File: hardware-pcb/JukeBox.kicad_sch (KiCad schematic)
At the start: 80 parts, among them J1 USB_C_Receptacle_USB2.0_16P, J2 Conn_01x04_Pin, Q1 Q_NPN_BEC, SW1 SW_SPST, SW10 SW_SPST, SW11 SW_SPST, SW12 SW_SPST, SW2 SW_SPST, SW3 SW_SPST, SW4 SW_SPST, SW5 SW_SPST, SW6 SW_SPST, SW7 SW_SPST, SW8 SW_SPST, SW9 SW_SPST, U1 NCP1117-3.3_SOT223, U2 W25Q64JVSSIQ-TR, U3 RP2040, U4 st7789v, U5 CAT24C512, Y2 ABM8-272-T3

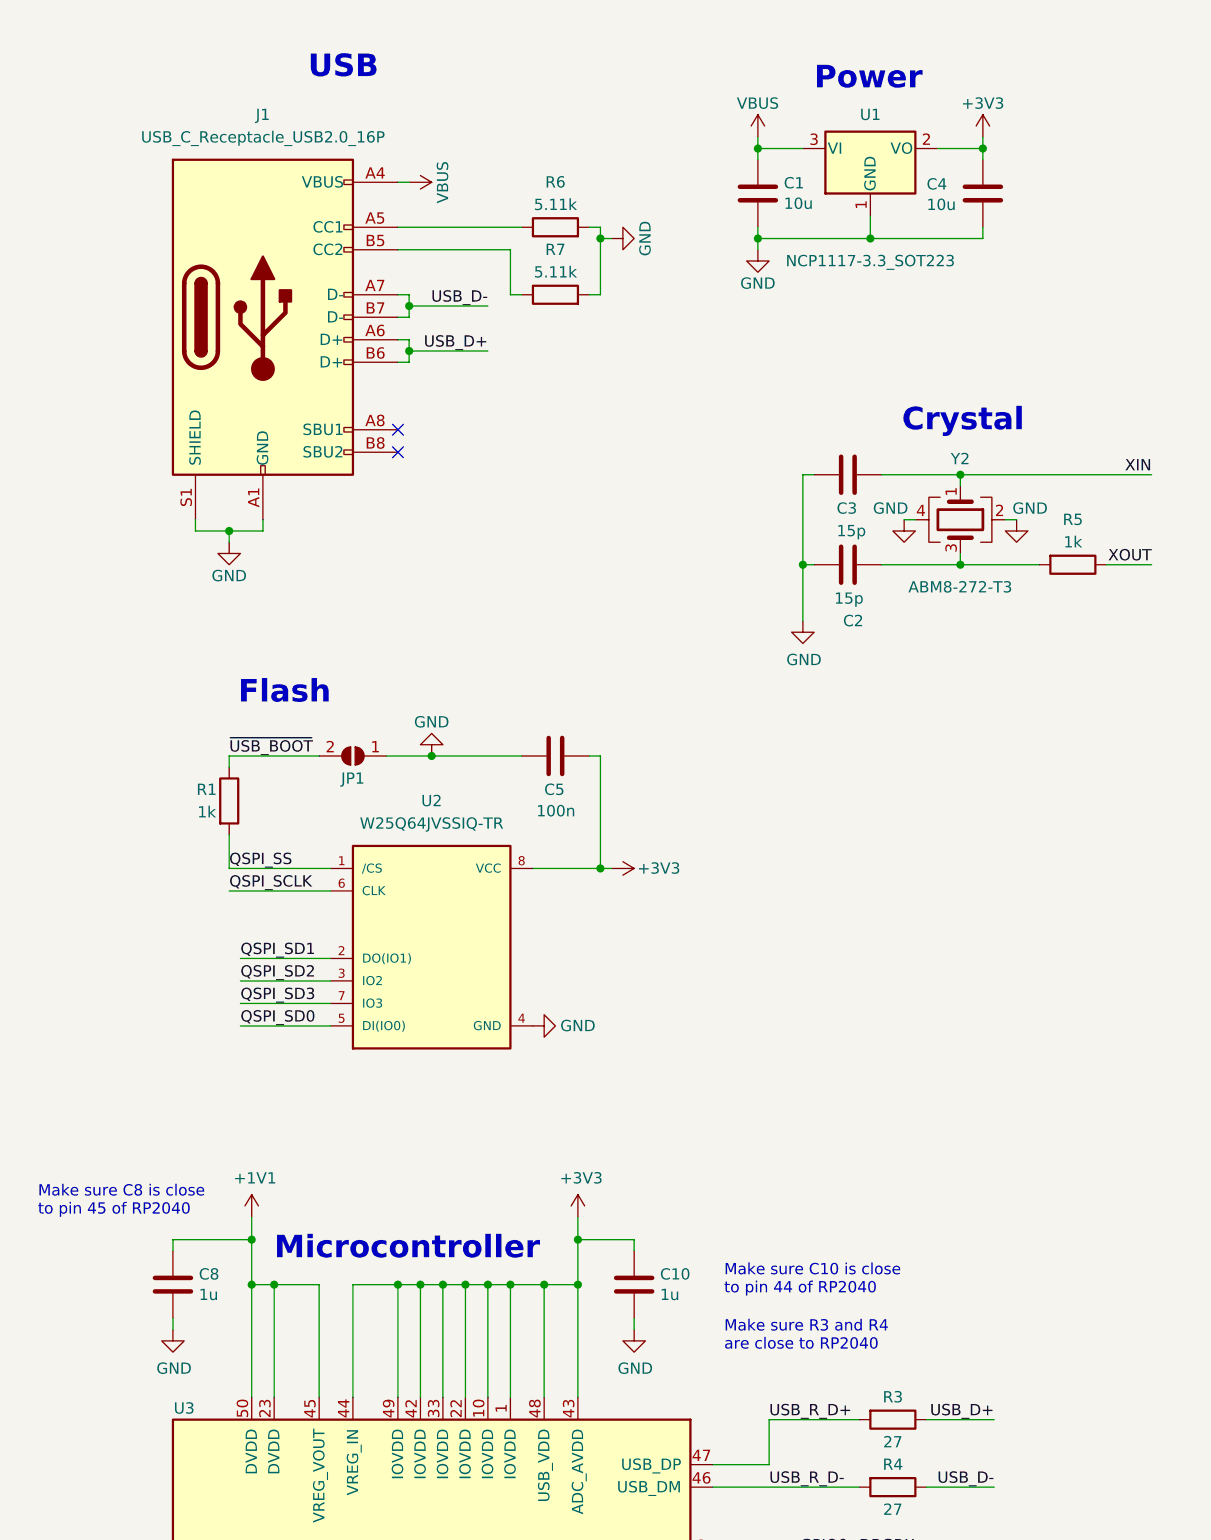
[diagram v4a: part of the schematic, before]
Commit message: update readmes, remove more redundant kicad elements
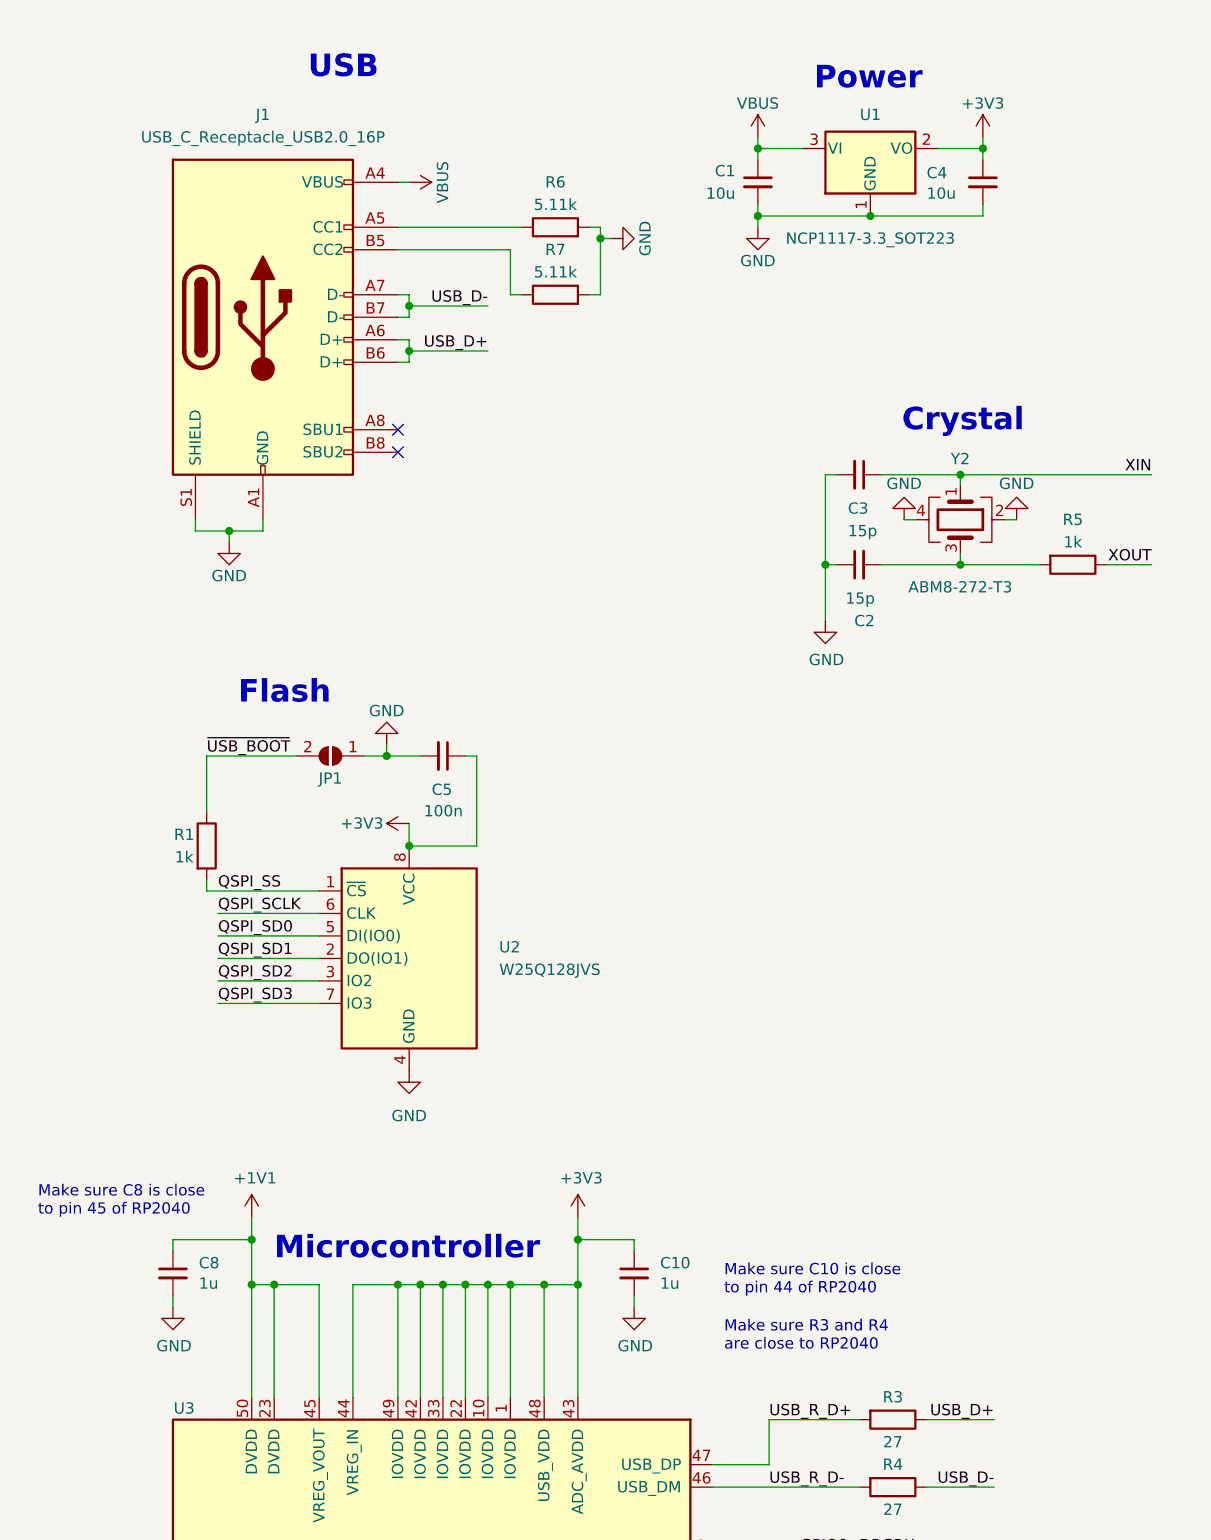
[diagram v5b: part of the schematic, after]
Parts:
- removed U2: W25Q64JVSSIQ-TR, Package_SO:SOIC-8W_5.3x5.3mm_P1.27mm, symbol W25Q64JVZPIQ-TR:W25Q64JVZPIQ-TR
- added U2: W25Q128JVS, Package_SO:SOIC-8_5.23x5.23mm_P1.27mm, symbol Memory_Flash:W25Q128JVS
- C1, C10, C2, C3, C4, C5, C8: symbol Device:C -> Device:C_Small
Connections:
- net +3V3: now also U2.8 (VCC)
- net GND: now also U2.4 (GND)
- net QSPI_SCLK: now also U2.6 (CLK)
- net QSPI_SD0: now also U2.5 (DI(IO0))
- net QSPI_SD1: now also U2.2 (DO(IO1))
- net QSPI_SD2: now also U2.3 (IO2)
- net QSPI_SD3: now also U2.7 (IO3)
- net QSPI_SS: now also U2.1 (~{CS})
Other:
- moved on the sheet: C1, C10, C2, C3, C4, C5, C8, JP1, R1

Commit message: update to rc design, update readme
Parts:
- removed J2: Conn_01x04_Pin, Connector_JST:JST_SH_SM04B-SRSS-TB_1x04-1MP_P1.00mm_Horizontal, symbol Connector:Conn_01x04_Pin
- removed R15: 10k, Resistor_SMD:R_0402_1005Metric, symbol Device:R
- removed R21, R22: 2k, Resistor_SMD:R_0402_1005Metric, symbol Device:R
- added TP1, TP2, TP21, TP22, TP23, TP24, TP25, TP26, TP27, TP3, TP31, TP32, TP4, TP41, TP42, TP5, TP51, TP52, TP53, TP54, TP55, TP56, TP6, TP7, TP8: TestPoint, TestPoint:TestPoint_Pad_D1.5mm, symbol Connector:TestPoint
- R12: value 600 -> 10k
- renumbered TP21 to TP14, TP22 to TP15, TP23 to TP16
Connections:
- net +3V3: now also C10.2; no longer C10.1
- net GND: now also C10.1, TP5.1, TP6.1, TP7.1, TP8.1; no longer C10.2
- net GPIO10: now also TP22.1
- net GPIO11: now also TP23.1
- net GPIO12: now also TP24.1
- net GPIO13: now also TP25.1
- net GPIO14: now also TP26.1
- net GPIO15: now also TP27.1
- net GPIO16: now also TP56.1
- net GPIO17: now also TP55.1
- net GPIO18: now also TP54.1
- net GPIO19: now also TP53.1
- net GPIO2: now also TP41.1
- net GPIO20: now also TP52.1
- net GPIO21: now also TP51.1
- net GPIO25: now also TP42.1
- net GPIO4: now also TP31.1
- net GPIO5: now also TP32.1
- net GPIO9: now also TP21.1
- net VBUS: now also TP1.1, TP2.1, TP3.1, TP4.1
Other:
- note added: "Clock Crystal"
- note added: "Make sure C8/C10 is close to pin 45/44 of RP2040"
- note removed: "Crystal"
- note removed: "Expansion"
- note removed: "Make sure C10 is close to pin 44 of RP2040"
- note removed: "Make sure C8 is close to pin 45 of RP2040"
- moved on the sheet: C1, C10, C2, C3, C4, C5, C8, D13, D14, D15, D16, D17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
